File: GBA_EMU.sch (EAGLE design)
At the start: 62 parts, among them Q1 MOSFET-PCHANNEL, SW1 LEFT, SW2 RIGHT, SW3 PWR_SWITCH, U1 RPI-ZERO, U2 FT230X, U3 MCP1642B-ADJ, U4 LM4875, U5 V_REG_LDOSMD2, U6 MIC7221, U7 AZV321, X1 LINK_SOCKET, X2 HEADPHONE

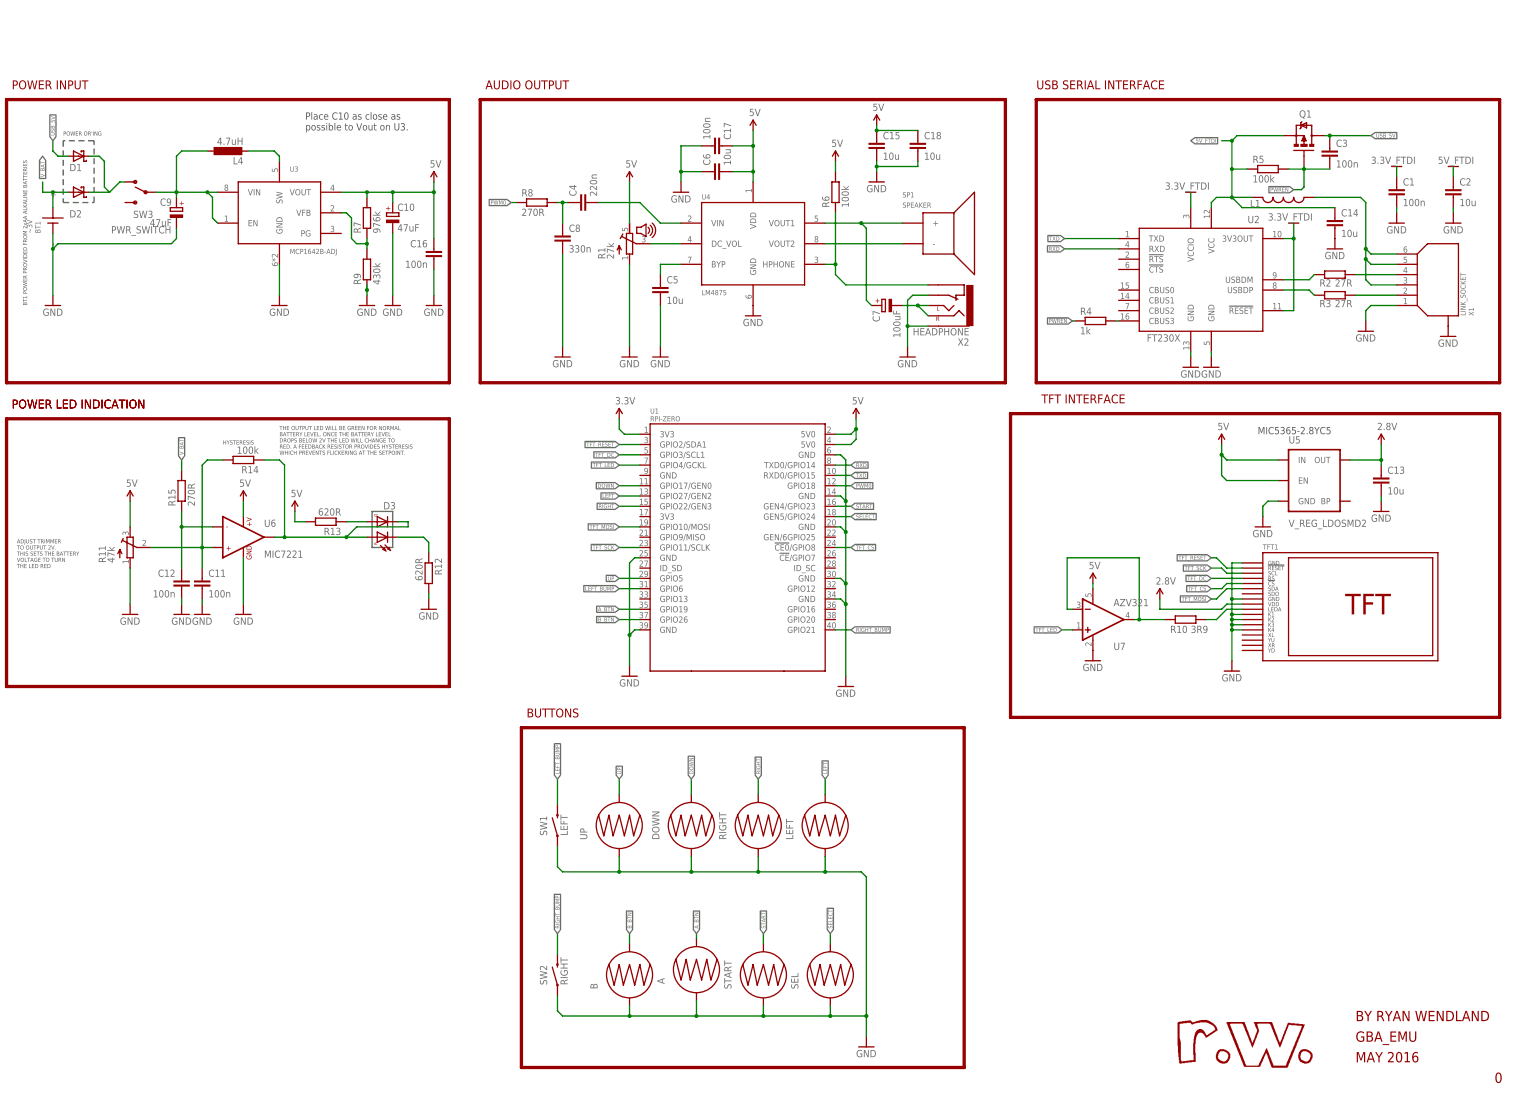
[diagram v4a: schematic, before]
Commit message: added coprocessor
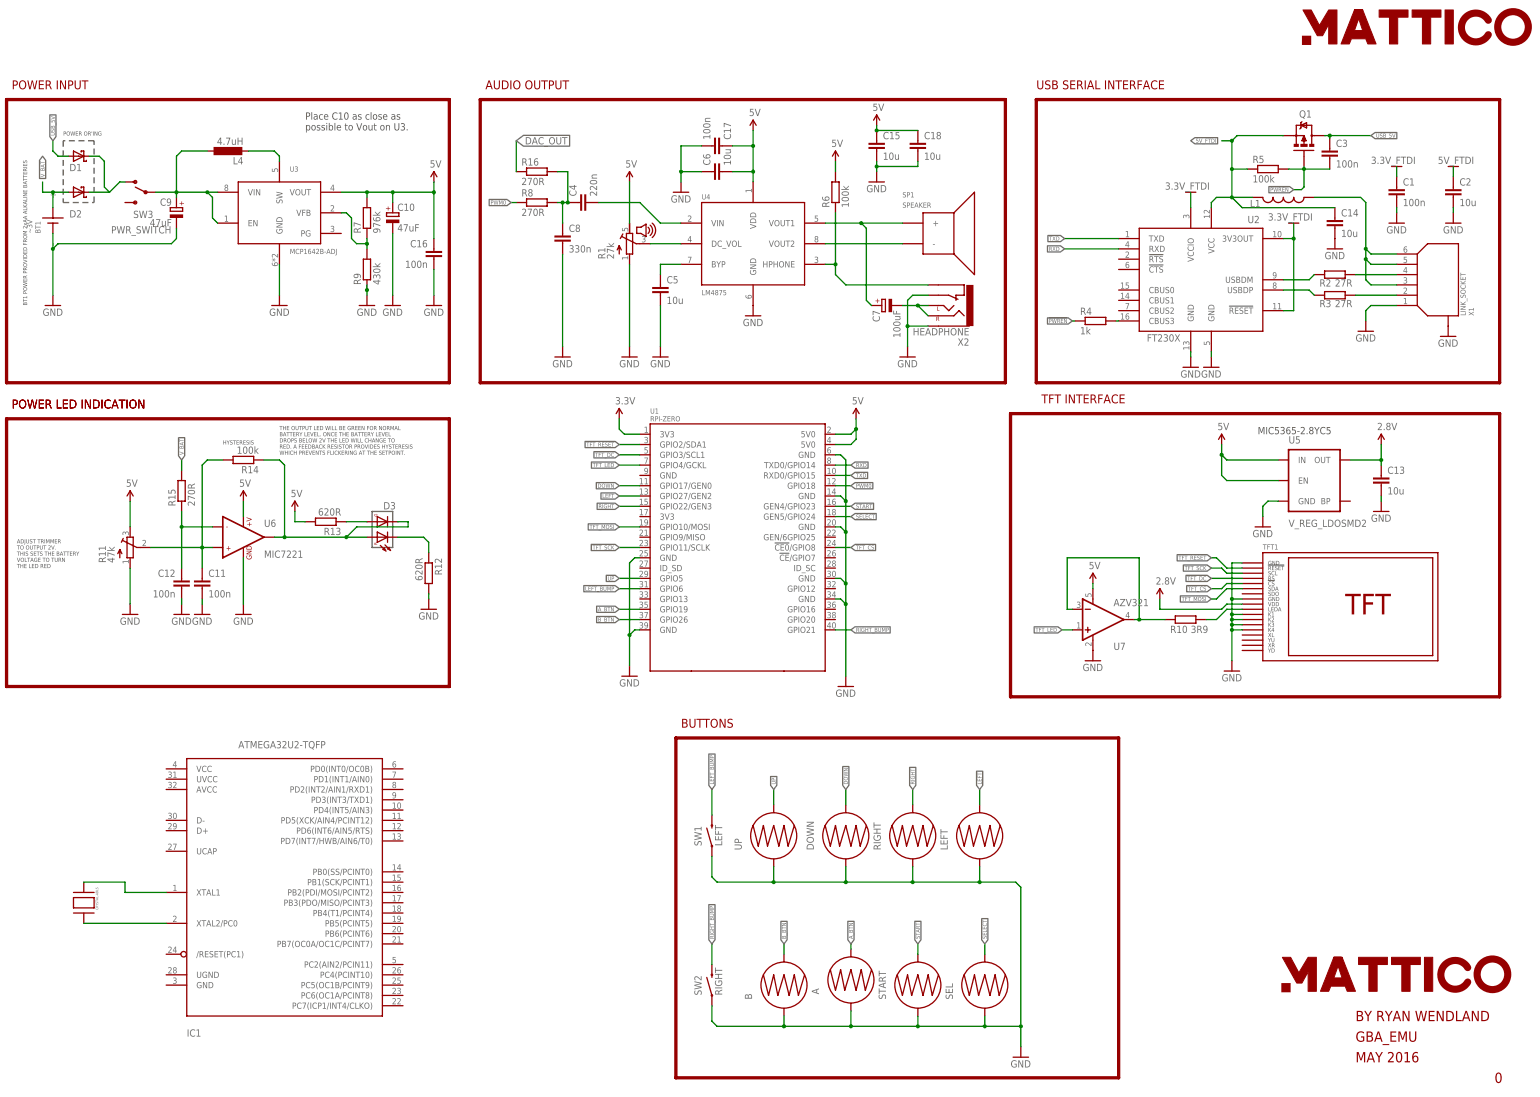
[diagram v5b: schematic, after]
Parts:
- added IC1: ATMEGA32U2-TQFP, adafruit:ATMEGA32U2-TQFP
- added R16: 270R, rcl:R-EU_R0805
- added U$1, U$2: LOGO2INCH_SVG, custom:LOGO2INCH_SVG
- added U$3: CRYSTAL-ABLS, custom:CRYSTAL-ABLS
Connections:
- new net DAC_OUT: R16.1
- new net N$17: IC1.XTAL1, U$3.P$2
- new net N$26: IC1.XTAL2/PC0, U$3.P$1
- net N$2: now also R16.2
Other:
- moved on the sheet: A, B, DOWN, LEFT, RIGHT, SEL, START, SW1, SW2, UP

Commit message: added AVR ISP
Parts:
- added C19, C20: 22pF, SparkFun-Capacitors:22PF-50V-5%(0603)
- added C21: 1uF, SparkFun-Capacitors:1UF-25V-10%(0805)"
- added D4: DIODE_DFLS130L, custom:DIODE_DFLS130L
- added ISP1: AVRISP-6, adafruit:AVRISP-6
- added U$4: CBT3244AD, custom:CBT3244AD
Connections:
- new net AVR_VCC: D4.C, IC1.AVCC, IC1.UVCC, IC1.VCC, ISP1.VCC
- new net COPRO_MISO: IC1.PB3(PDO/MISO/PCINT3), ISP1.MISO
- new net COPRO_MOSI: IC1.PB2(PDI/MOSI/PCINT2), ISP1.MOSI
- new net COPRO_SCK: IC1.PB1(SCK/PCINT1), ISP1.SCK
- new net N$28: C21.1, IC1.UCAP
- new net RESET: IC1./RESET(PC1), ISP1.RST
- net 5V: now also D4.A
- net GND: now also C19.2, C20.2, C21.2, IC1.GND, ISP1.GND
- net N$17: now also C20.1
- net N$26: now also C19.1
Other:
- note added: "Bus Switch"
- note added: "Maybe need to reroute/redo the power here"

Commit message: switched to USB-mini :/
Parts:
- removed U$4: CBT3244AD, custom:CBT3244AD
- removed X1: LINK_SOCKET, GBA:LINK_SOCKET
- added CN1: (no value), adafruit:USBMINIB
- added J1: (no value), SparkFun-Connectors:M041.27MM
- added U$5: MCP48FEB01-E/UN, custom:MCP48FEB01-E/UN
- IC1: value ATMEGA32U2-TQFP -> MEGA16U2
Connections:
- new net DAC_CS: IC1.PD7(INT7/HWB/AIN6/T0), U$5.CS
- new net DAC_REF: U$5.VREF
- new net N$27: IC1.PD3(INT3/TXD1), J1.2
- new net N$29: IC1.PD2(INT2/AIN1/RXD1), J1.1
- net 5V: now also U$5.VDD
- net AVR_VCC: now also J1.3
- net COPRO_MISO: now also U$5.SDO
- net COPRO_MOSI: now also U$5.SDI
- net COPRO_SCK: now also U$5.SCLK
- net DAC_OUT: now also U$5.VOUT
- net GND: now also CN1.GND, J1.4, U$5.VSS; no longer X1.1, X1.GND
- net N$3: now also CN1.VBUS; no longer X1.3, X1.5, X1.6
- net N$4: now also CN1.D-; no longer X1.4
- net N$5: now also CN1.D+; no longer X1.2

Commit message: added some descriptions and moved some labels
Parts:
- added R17: 4.7k, rcl:R-EU_R0805
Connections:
- net N$27 renamed COPRO_TX
- net N$29 renamed COPRO_RX
- net AVR_VCC: now also R17.2
- net RESET: now also R17.1
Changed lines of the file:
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@@
 <part name="GND6" library="SparkFun-Aesthetics" deviceset="GND" device=""/>
 <part name="J1" library="SparkFun-Connectors" deviceset="M04" device="1.27MM"/>
+<part name="R17" library="rcl" deviceset="R-EU_" device="R0805" value="4.7k"/>
 </parts>
 <sheets>
@@
 <instance part="GND6" gate="1" x="317.5" y="17.78"/>
 <instance part="J1" gate="G$1" x="322.58" y="33.02" rot="R180"/>
+<instance part="R17" gate="G$1" x="292.1" y="-10.16" rot="R90"/>
 </instances>
 <busses>
@@
 <label x="264.16" y="-30.48" size="1.778" layer="95" rot="R180" xref="yes"/>
 </segment>
+<segment>
+<wire x1="292.1" y1="-15.24" x2="299.72" y2="-15.24" width="0.1524" layer="91"/>
+<label x="299.72" y="-15.24" size="1.778" layer="95" xref="yes"/>
+<pinref part="R17" gate="G$1" pin="1"/>
+</segment>
 </net>
 <net name="AVR_VCC" class="0">
@@
 <pinref part="J1" gate="G$1" pin="3"/>
 </segment>
+<segment>
+<wire x1="292.1" y1="-5.08" x2="299.72" y2="-5.08" width="0.1524" layer="91"/>
+<label x="299.72" y="-5.08" size="1.778" layer="95" xref="yes"/>
+<pinref part="R17" gate="G$1" pin="2"/>
+</segment>
 </net>
 <net name="COPRO_MOSI" class="0">
@@
 </segment>
 </net>
-<net name="N$27" class="0">
+<net name="COPRO_TX" class="0">
 <segment>
 <pinref part="IC1" gate="G$1" pin="PD3(INT3/TXD1)"/>
 <wire x1="279.4" y1="33.02" x2="317.5" y2="33.02" width="0.1524" layer="91"/>
 <pinref part="J1" gate="G$1" pin="2"/>
-</segment>
-</net>
-<net name="N$29" class="0">
+<label x="299.72" y="33.02" size="1.778" layer="95" rot="R180"/>
+</segment>
+</net>
+<net name="COPRO_RX" class="0">
 <segment>
 <pinref part="IC1" gate="G$1" pin="PD2(INT2/AIN1/RXD1)"/>
 <wire x1="279.4" y1="35.56" x2="317.5" y2="35.56" width="0.1524" layer="91"/>
 <pinref part="J1" gate="G$1" pin="1"/>
-</segment>
-</net>
+<label x="307.34" y="38.1" size="1.778" layer="95" rot="R180"/>
+</segment>
+</net>
